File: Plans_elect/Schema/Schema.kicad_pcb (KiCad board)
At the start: 2 copper layers, 11 x 0.6 mm, 23 parts, among them J1 Conn_01x22, J2 Conn_01x22, J3 Conn_01x10, J4 Conn_01x14, SW1 RotaryEncoder_Switch, SW2 RotaryEncoder_Switch, SW3 RotaryEncoder

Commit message: plan mec avancer + tit peu delect
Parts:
- moved R3 110.5 mm to (99.0, 88.5), turned to 90 degrees
- moved R1 104.1 mm to (105.5, 88.5), turned to 90 degrees
- moved C2 99.6 mm to (105.5, 95.5), turned to 90 degrees
- moved R2 98.0 mm to (111.5, 88.5), turned to 90 degrees
- moved C1 93.9 mm to (111.5, 95.5), turned to -90 degrees
- moved R12 87.9 mm to (129.0, 108.5), turned to 90 degrees
- moved R11 86.8 mm to (129.0, 100.5), turned to -90 degrees
- moved C6 78.9 mm to (129.0, 115.5), turned to -90 degrees
- moved R10 74.6 mm to (135.5, 108.5), turned to 90 degrees
- moved J3 74.2 mm to (165.5, 53.5)
- moved R9 74.2 mm to (135.5, 101.0), turned to 90 degrees
- moved C5 73.7 mm to (135.5, 115.5), turned to -90 degrees
- moved SW3 46.6 mm to (145.5, 113.0), turned to 90 degrees
- moved R13 43.8 mm to (170.5, 92.0), turned to -90 degrees
- moved J2 43.6 mm to (153.0, 72.0), turned to -90 degrees
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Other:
- board size 11 x 0.6 mm -> 0.6 x 11 mm

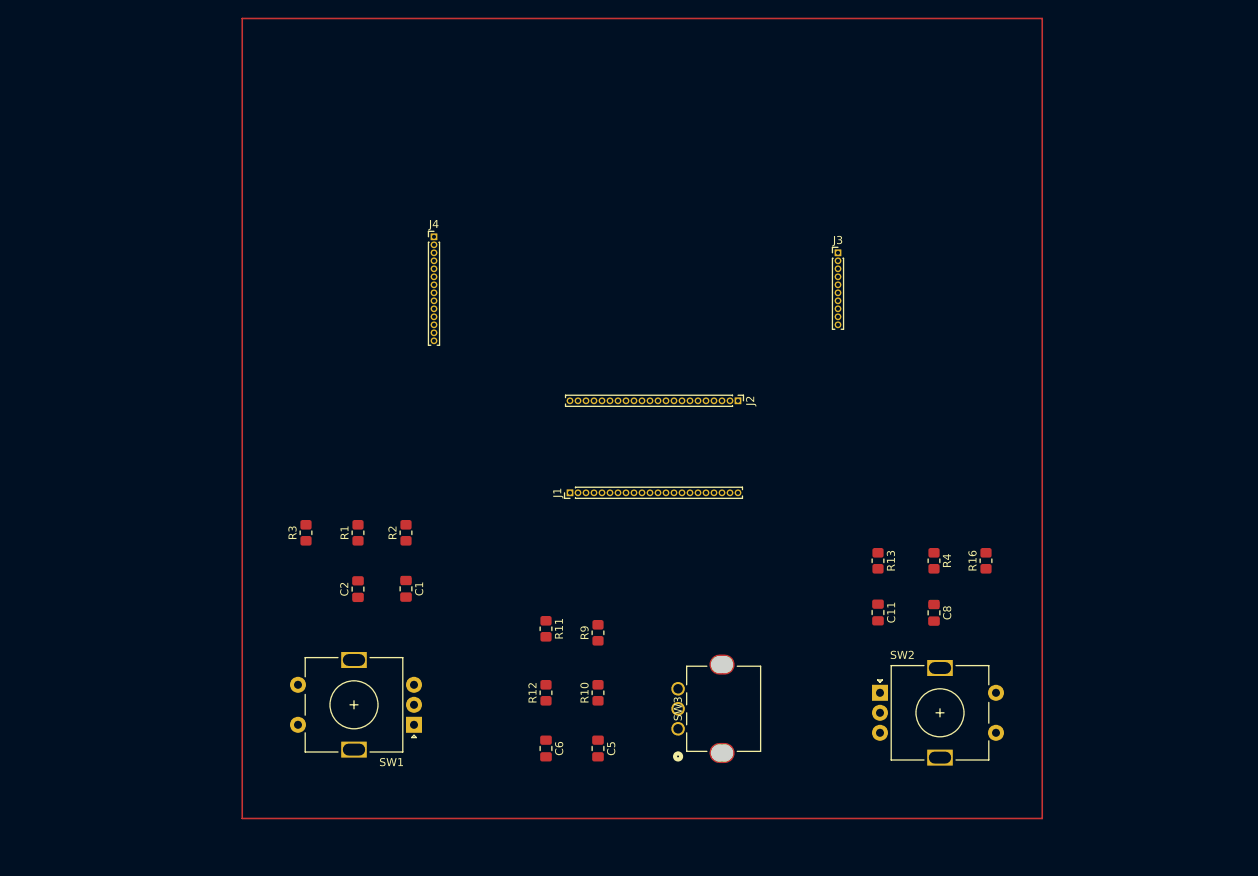
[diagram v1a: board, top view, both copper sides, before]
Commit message: Plan elect finit
il y a 16 erreurs mais les 16 c'est sur le fait que jai essayer de faire mon propre footprint pis ca fait nimporte quoi
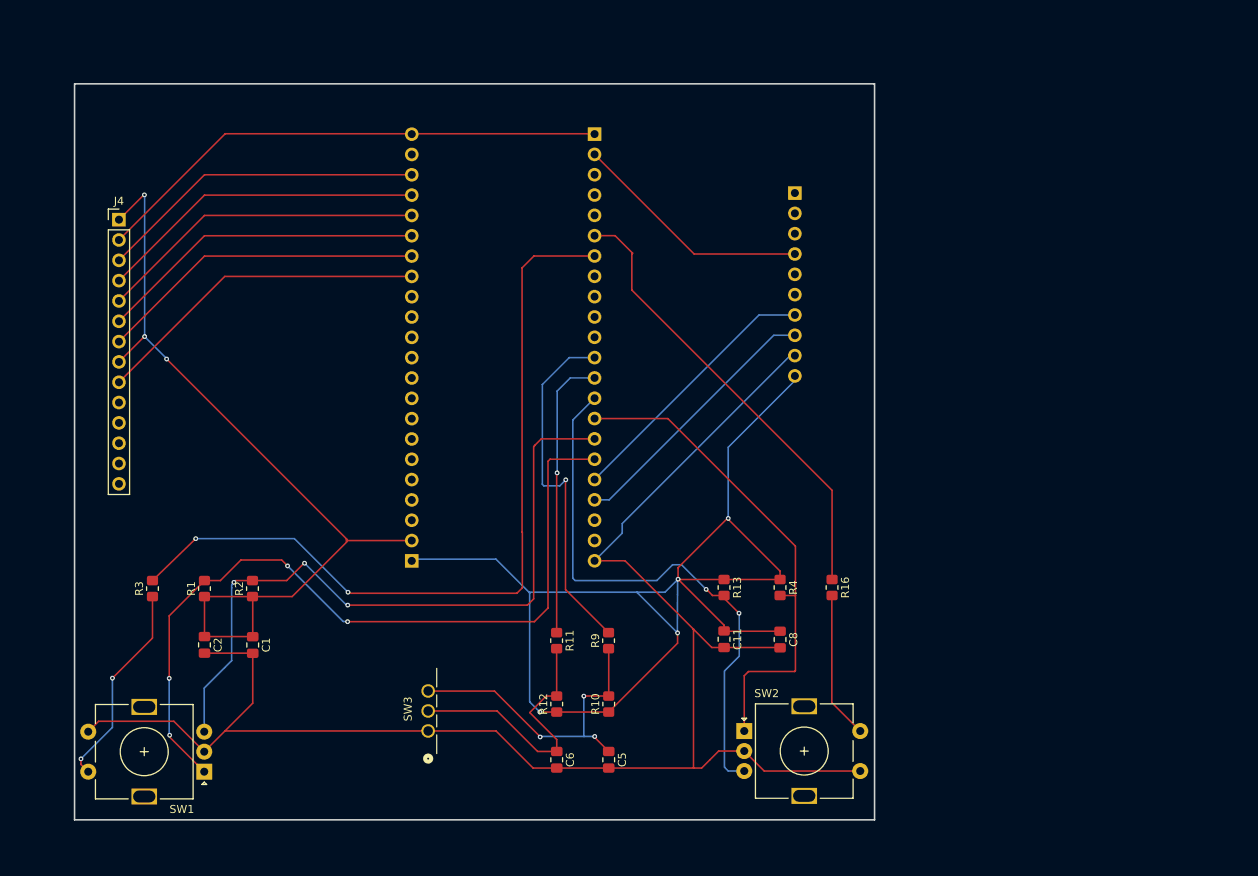
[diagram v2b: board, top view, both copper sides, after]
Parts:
- J1, J2: footprint Connector_PinHeader_1.00mm:PinHeader_1x22_P1.00mm_Vertical -> Connector_PinHeader_2.54mm:PinHeader_1x22_P2.54mm_Vertical; moved to B.Cu
- J3: footprint Connector_PinHeader_1.00mm:PinHeader_1x10_P1.00mm_Vertical -> Connector_PinHeader_2.54mm:PinHeader_1x10_P2.54mm_Vertical; moved to B.Cu
- J4: footprint Connector_PinHeader_1.00mm:PinHeader_1x14_P1.00mm_Vertical -> Connector_PinHeader_2.54mm:PinHeader_1x14_P2.54mm_Vertical
- moved J4 39.4 mm to (75.6, 49.4)
- moved J2 37.9 mm to (135.1, 38.7), turned to 180 degrees
- moved SW3 31.2 mm to (114.3, 113.3)
- moved SW1 26.9 mm to (86.3, 118.4)
- moved J1 21.5 mm to (112.2, 92.0), turned to 0 degrees
- moved C2 20.4 mm to (86.3, 102.5), turned to -90 degrees
- moved R1 20.4 mm to (86.3, 95.5)
- moved R2 20.4 mm to (92.3, 95.5)
- moved R3 20.4 mm to (79.8, 95.5)
- moved C1 20.4 mm to (92.3, 102.5)
- moved C11 19.5 mm to (151.3, 101.8)
- moved C8 19.5 mm to (158.3, 101.8)
- moved R13 19.5 mm to (151.3, 95.3)
- moved R16 19.5 mm to (164.8, 95.3), turned to -90 degrees
- moved R4 19.5 mm to (158.3, 95.3)
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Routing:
- net GND: track 0.00 -> 297.6 mm
- net 3V3: track 0.00 -> 266.4 mm, vias 0 -> 7
- net /GPIO48-BSW1: track 0.00 -> 101.5 mm, vias 0 -> 2
- net /GPIO42-chA_X: track 0.00 -> 100.0 mm, vias 0 -> 4
- net /GPIO41-chB_X: track 0.00 -> 88.7 mm, vias 0 -> 3
- net /GPIO39-chB_Y: track 0.00 -> 71.4 mm, vias 0 -> 2
- net /GPIO40-chA_Y: track 0.00 -> 62.8 mm
- net /GPIO47-BSW2: track 0.00 -> 56.9 mm
- net /GPIO37-chB_S: track 0.00 -> 45.1 mm, vias 0 -> 1
- net /GPIO9-SDO: track 0.00 -> 42.2 mm
- net /GPIO12-DC: track 0.00 -> 41.2 mm
- net /GPIO14-CS: track 0.00 -> 41.2 mm
- net /GPIO13-RESET: track 0.00 -> 41.2 mm
- net /GPIO11-SDI: track 0.00 -> 41.2 mm
- net /GPIO10-SCk: track 0.00 -> 41.2 mm
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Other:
- board size 0.6 x 11 mm -> 100 x 92 mm
- board text added: "Triangles des bernardes"

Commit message: FIX ET ADD QUELQUES TRUCS
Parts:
- added kibuzzard-66ACC153: G***, kibuzzard-66ACC153, F.Cu at (72.7, 51.9)
- added kibuzzard-66ACC153: G***, kibuzzard-66ACC153, F.Cu at (109.5, 38.6)
- added kibuzzard-66ACC180: G***, kibuzzard-66ACC180, F.Cu at (138.0, 38.7)
- added kibuzzard-66ACC180: G***, kibuzzard-66ACC180, F.Cu at (138.1, 41.1)
- added kibuzzard-66ACC180: G***, kibuzzard-66ACC180, F.Cu at (163.0, 66.3)
- added kibuzzard-66ACC180: G***, kibuzzard-66ACC180, F.Cu at (163.0, 53.6)
- added kibuzzard-66ACC1A1: G***, kibuzzard-66ACC1A1, F.Cu at (109.8, 41.3)
- added kibuzzard-66ACC1C4: G***, kibuzzard-66ACC1C4, F.Cu at (107.2, 46.3)
- added kibuzzard-66ACC1D0: G***, kibuzzard-66ACC1D0, F.Cu at (107.5, 48.8)
- added kibuzzard-66ACC1F2: G***, kibuzzard-66ACC1F2, F.Cu at (107.5, 43.8)
- added kibuzzard-66ACC204: G***, kibuzzard-66ACC204, F.Cu at (107.2, 51.4)
- added kibuzzard-66ACC21E: G***, kibuzzard-66ACC21E, F.Cu at (107.2, 53.9)
- added kibuzzard-66ACC22A: G***, kibuzzard-66ACC22A, F.Cu at (107.2, 56.5)
- added kibuzzard-66ACC25D: G***, kibuzzard-66ACC25D, F.Cu at (72.8, 67.2)
- added kibuzzard-66ACC25D: G***, kibuzzard-66ACC25D, F.Cu at (72.8, 49.4)
- added kibuzzard-66ACC25D: G***, kibuzzard-66ACC25D, F.Cu at (109.3, 92.1)
- added kibuzzard-66ACC25D: G***, kibuzzard-66ACC25D, F.Cu at (109.3, 89.5)
- added kibuzzard-66ACC281: G***, kibuzzard-66ACC281, F.Cu at (138.0, 92.0)
- added kibuzzard-66ACC2A7: G***, kibuzzard-66ACC2A7, F.Cu at (140.2, 51.4)
- added kibuzzard-66ACC2A7: G***, kibuzzard-66ACC2A7, F.Cu at (140.3, 71.5)
- added kibuzzard-66ACC2A7: G***, kibuzzard-66ACC2A7, F.Cu at (140.2, 74.2)
- added kibuzzard-66ACC2DC: G***, kibuzzard-66ACC2DC, F.Cu at (139.8, 79.4)
- added kibuzzard-66ACC2DC: G***, kibuzzard-66ACC2DC, F.Cu at (139.8, 54.0)
- added kibuzzard-66ACC2DC: G***, kibuzzard-66ACC2DC, F.Cu at (139.8, 76.8)
- added kibuzzard-66ACC309: G***, kibuzzard-66ACC309, F.Cu at (140.8, 69.2)
- added kibuzzard-66ACC309: G***, kibuzzard-66ACC309, F.Cu at (141.0, 66.6)
- added kibuzzard-66ACC392: G***, kibuzzard-66ACC392, F.Cu at (165.2, 63.7)
- added kibuzzard-66ACC392: G***, kibuzzard-66ACC392, F.Cu at (140.2, 84.5)
- added kibuzzard-66ACC3A5: G***, kibuzzard-66ACC3A5, F.Cu at (140.2, 81.9)
- added kibuzzard-66ACC3A5: G***, kibuzzard-66ACC3A5, F.Cu at (165.2, 61.1)
- added kibuzzard-66ACC438: G***, kibuzzard-66ACC438, F.Cu at (80.4, 54.3)
- added kibuzzard-66ACC45C: G***, kibuzzard-66ACC45C, F.Cu at (80.7, 57.0)
- added kibuzzard-66ACC46C: G***, kibuzzard-66ACC46C, F.Cu at (80.5, 59.5)
- added kibuzzard-66ACC47C: G***, kibuzzard-66ACC47C, F.Cu at (80.7, 62.0)
- added kibuzzard-66ACC49B: G***, kibuzzard-66ACC49B, F.Cu at (80.7, 64.7)
- added kibuzzard-66ACC4A4: G***, kibuzzard-66ACC4A4, F.Cu at (80.7, 69.8)
- added kibuzzard-66ACC4E0: G***, kibuzzard-66ACC4E0, F.Cu at (163.1, 69.0)
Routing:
- net 3V3: track 266.4 -> 269.0 mm
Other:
- board text added: "ETCH A SKETCH"
- board text added: "PCB fait par: Charles-Ariel Dion Jordan Gagnon Dans le contexte: CCI U de S"

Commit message: push holed
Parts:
- added REF**: MountingHole_3.2mm_M3, MountingHole:MountingHole_3.2mm_M3, F.Cu at (91.3, 120.8)
- added REF**: MountingHole_3.2mm_M3, MountingHole:MountingHole_3.2mm_M3, F.Cu at (148.7, 120.8)
- added REF**: MountingHole_3.2mm_M3, MountingHole:MountingHole_3.2mm_M3, F.Cu at (73.7, 35.9)
- added REF**: MountingHole_3.2mm_M3, MountingHole:MountingHole_3.2mm_M3, F.Cu at (166.5, 35.9)
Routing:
- net GND: track 297.6 -> 296.4 mm

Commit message: push gnd et nouveau gerber
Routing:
- added copper zone on B.Cu, net GND
- added copper zone on F.Cu, net GND
